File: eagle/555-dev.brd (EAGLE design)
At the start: 50 x 50 mm, 28 parts, among them IC1 NE555, Q1 IRF740, T1 2N2222

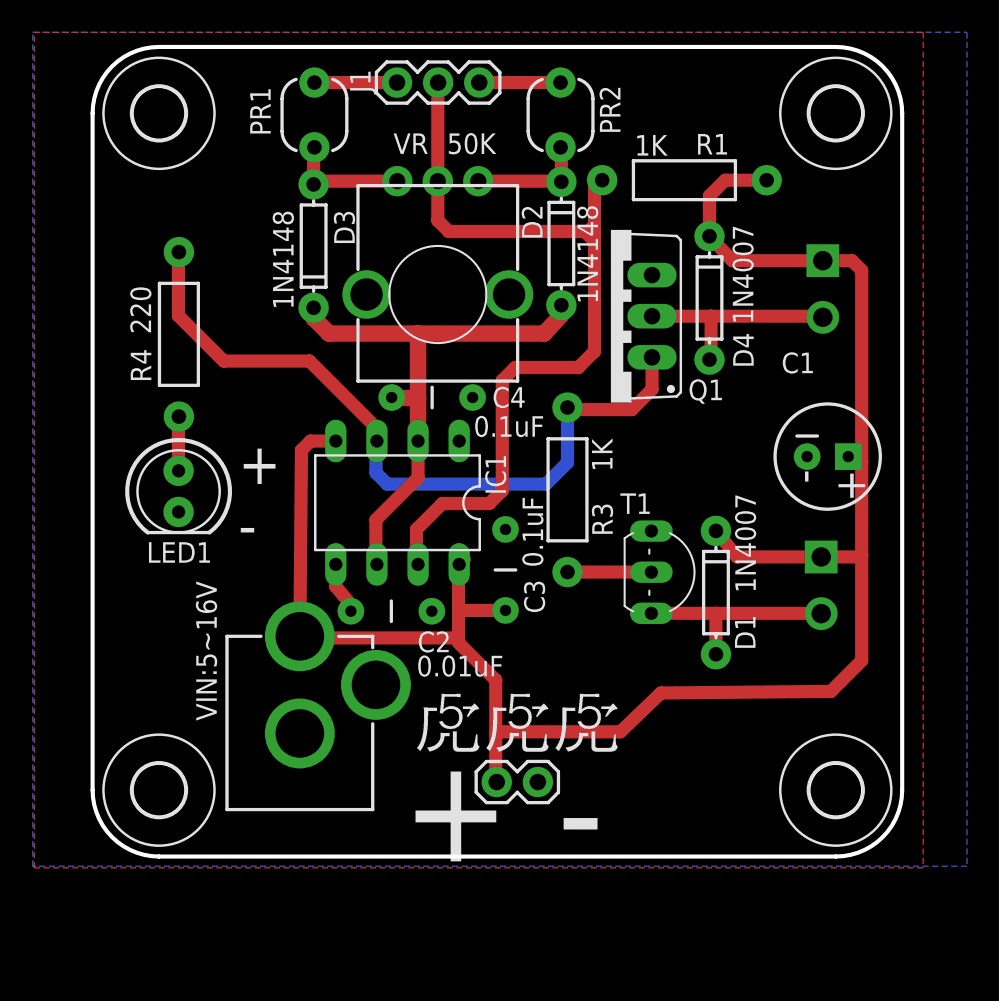
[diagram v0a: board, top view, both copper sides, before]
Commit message: add R2 base resistor and change Q1 into TIP120/IRF740
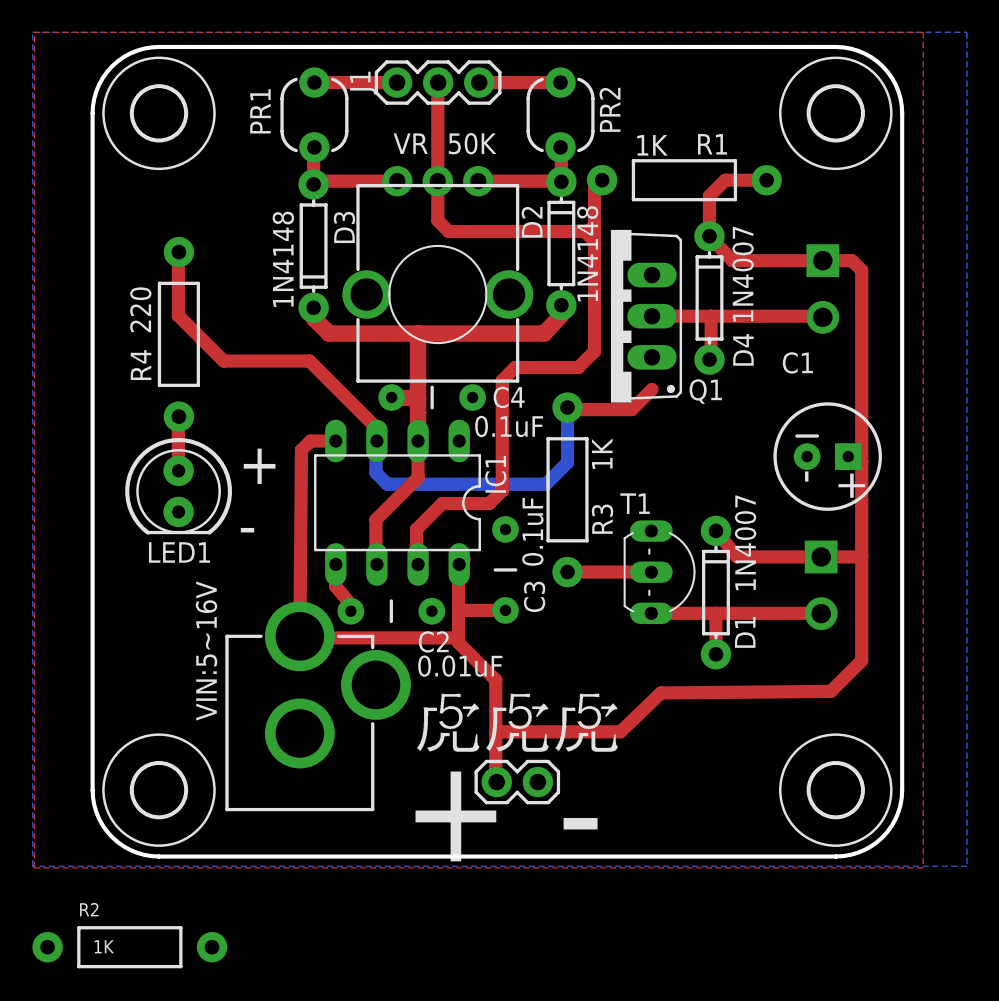
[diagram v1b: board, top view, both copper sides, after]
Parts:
- added R2: 1K, SparkFun-Resistors:AXIAL-0.4
- Q1: value IRF740 -> IRF740/TIP120
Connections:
- new net N$1: Q1.G, R2.P$1
- net OUT: now also R2.P$2; no longer Q1.G
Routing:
- net OUT: track 45.7 -> 43.7 mm
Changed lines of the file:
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@@
 <?xml version="1.0" encoding="utf-8"?>
 <!DOCTYPE eagle SYSTEM "eagle.dtd">
-<eagle version="7.4.0">
+<eagle version="7.2.0">
 <drawing>
 <settings>
@@
 <attribute name="VALUE" x="3.5066" y="19.3496" size="1.27" layer="27" ratio="10" rot="R270"/>
 </element>
-<element name="Q1" library="transistor-power" package="TO220BV" value="IRF740" x="32.01" y="33.37" smashed="yes" rot="R90">
+<element name="Q1" library="transistor-power" package="TO220BV" value="IRF740/TIP120" x="32.01" y="33.37" smashed="yes" rot="R90">
 <attribute name="NAME" x="39.01" y="29.4552" size="1.27" layer="25" font="vector" ratio="10" rot="R180"/>
 <attribute name="VALUE" x="39.01" y="27.63" size="1.27" layer="27" font="vector" ratio="10" rot="R180"/>
@@
 </element>
 <element name="U$1" library="SparkFun-Electromechanical" package="LOGO" value="LOGO" x="19.8" y="6.3"/>
+<element name="R2" library="SparkFun-Resistors" package="AXIAL-0.4" value="1K" x="2.3" y="-5.6"/>
 </elements>
 <signals>
@@
 <contactref element="R4" pad="P$2"/>
 <contactref element="R3" pad="P$2"/>
-<contactref element="Q1" pad="G"/>
-<wire x1="34.55" y1="30.83" x2="34.55" y2="28.85" width="0.8128" layer="1"/>
 <wire x1="34.55" y1="28.85" x2="33.3" y2="27.6" width="0.8128" layer="1"/>
 <wire x1="33.3" y1="27.6" x2="29.46" y2="27.6" width="0.8128" layer="1"/>
@@
 <wire x1="17.6" y1="26.4" x2="17.6" y2="25.7" width="0.8128" layer="1"/>
 <wire x1="17.6" y1="25.7" x2="17.56" y2="25.66" width="0.8128" layer="1"/>
+<contactref element="R2" pad="P$2"/>
+<wire x1="7.38" y1="-5.6" x2="18.2" y2="23" width="0" layer="19" extent="16-16"/>
 </signal>
 <signal name="GND">
@@
 <wire x1="23.88" y1="47.8" x2="28.9" y2="47.8" width="0.8128" layer="1"/>
 </signal>
+<signal name="N$1">
+<contactref element="Q1" pad="G"/>
+<contactref element="R2" pad="P$1"/>
+<wire x1="-2.78" y1="-5.6" x2="34.55" y2="30.83" width="0" layer="19" extent="1-1"/>
+</signal>
 </signals>

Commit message: added base R
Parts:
- removed PR1, PR2: PHOTOCELLPTH-KIT, SparkFun-Sensors:PHOTOCELL-KIT
- added R5, R6: (no value), Discrete:0546/3.3
- JP1, JP2: device SparkFun-Connectors:SCREWTERMINAL-3.5MM-2-NS -> SparkFun-Connectors:1X02_2.54_SCREWTERM
- moved R2 45.4 mm to (34.7, 26.2), turned to 180 degrees
- moved U$1 10.6 mm to (28.7, 0.60)
- moved R3 6.51 mm to (29.6, 16.1)
- moved T1 1.40 mm to (35.8, 16.2)
- moved JP1 0.60 mm to (44.4, 18.5)
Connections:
- net LOAD1-: now also JP1.P1; no longer JP1.2
- net LOAD2-: now also JP2.P1; no longer JP2.2
- net N$2: now also R6.P$1; no longer PR2.1
- net N$3: now also R5.P$1; no longer PR1.1
- net PR1: now also R5.P$2; no longer PR1.2
- net PR2: now also R6.P$2; no longer PR2.2
- net VCC: now also JP1.P2, JP2.P2; no longer JP1.1, JP2.1
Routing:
- net N$1: track 0.00 -> 9.34 mm
- net N$7: track 5.18 -> 10.4 mm
- net LOAD1-: track 13.0 -> 11.8 mm
- net OUT: track 43.7 -> 42.6 mm
- net LOAD2-: track 13.3 -> 14.1 mm
